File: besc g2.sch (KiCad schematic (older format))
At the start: 15 parts

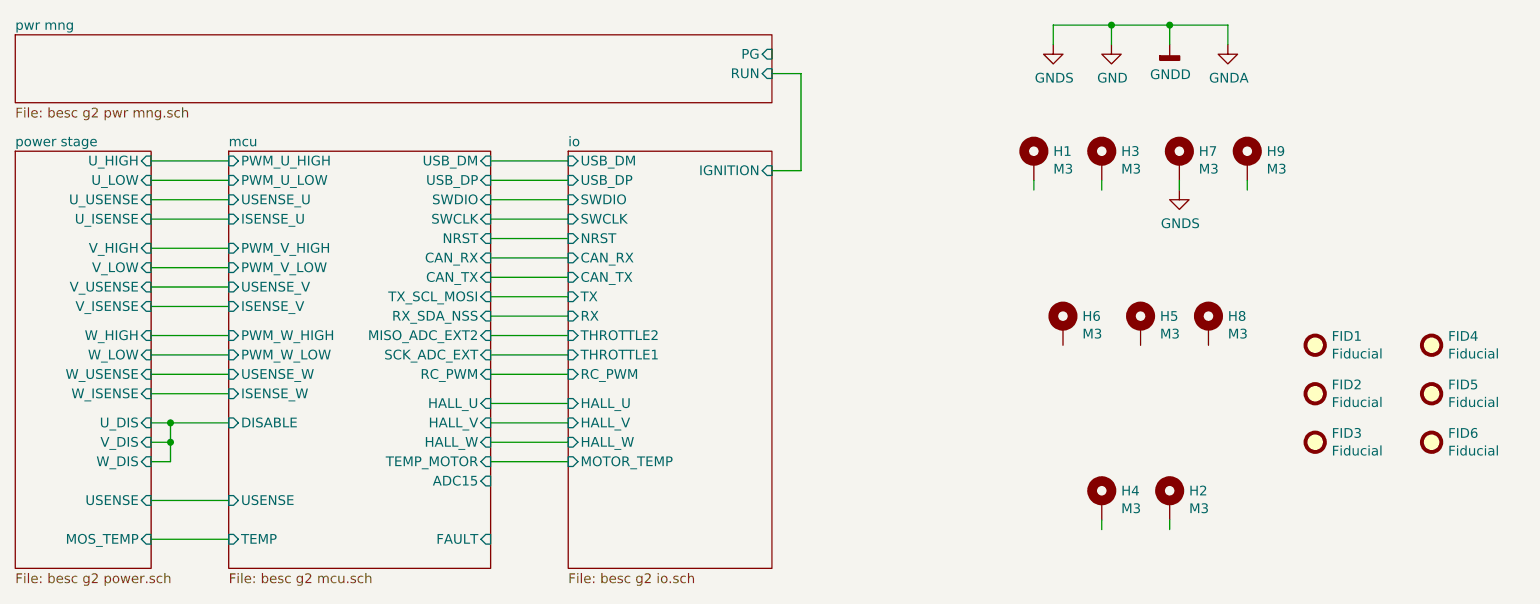
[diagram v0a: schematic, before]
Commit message: Added brakes, i2c
Signed-off-by: manianac <manianac@gmail.com>
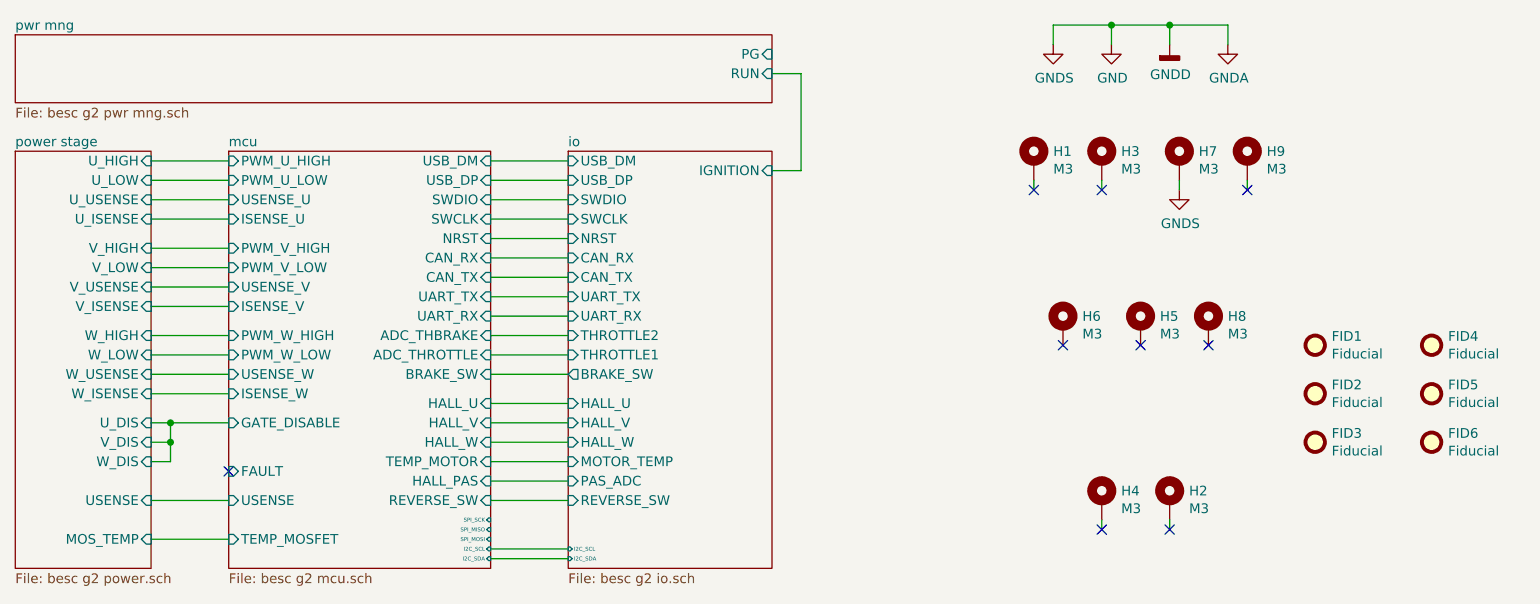
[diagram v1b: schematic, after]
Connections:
- wire segments 52 -> 56
- no-connect marks 0 -> 9
